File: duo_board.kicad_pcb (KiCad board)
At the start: 2 copper layers, 167 x 122.9 mm, 49 parts, among them J1 PJ-342B-TX-SMT, U1 STM32F103RCTx

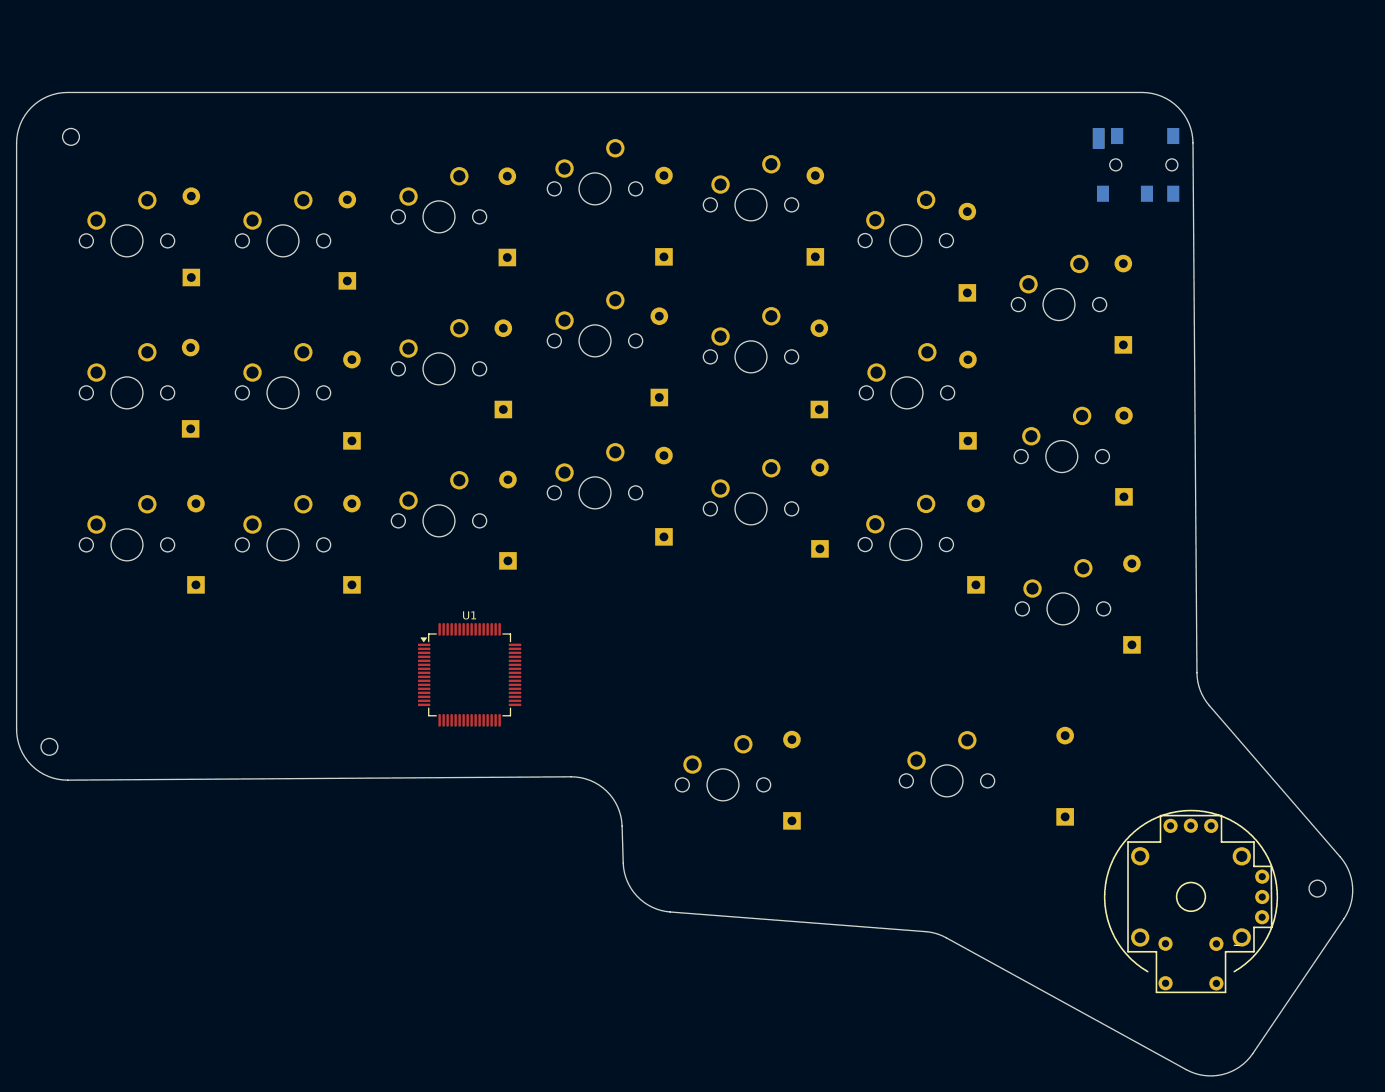
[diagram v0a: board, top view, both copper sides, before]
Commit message: completed MCU power supply
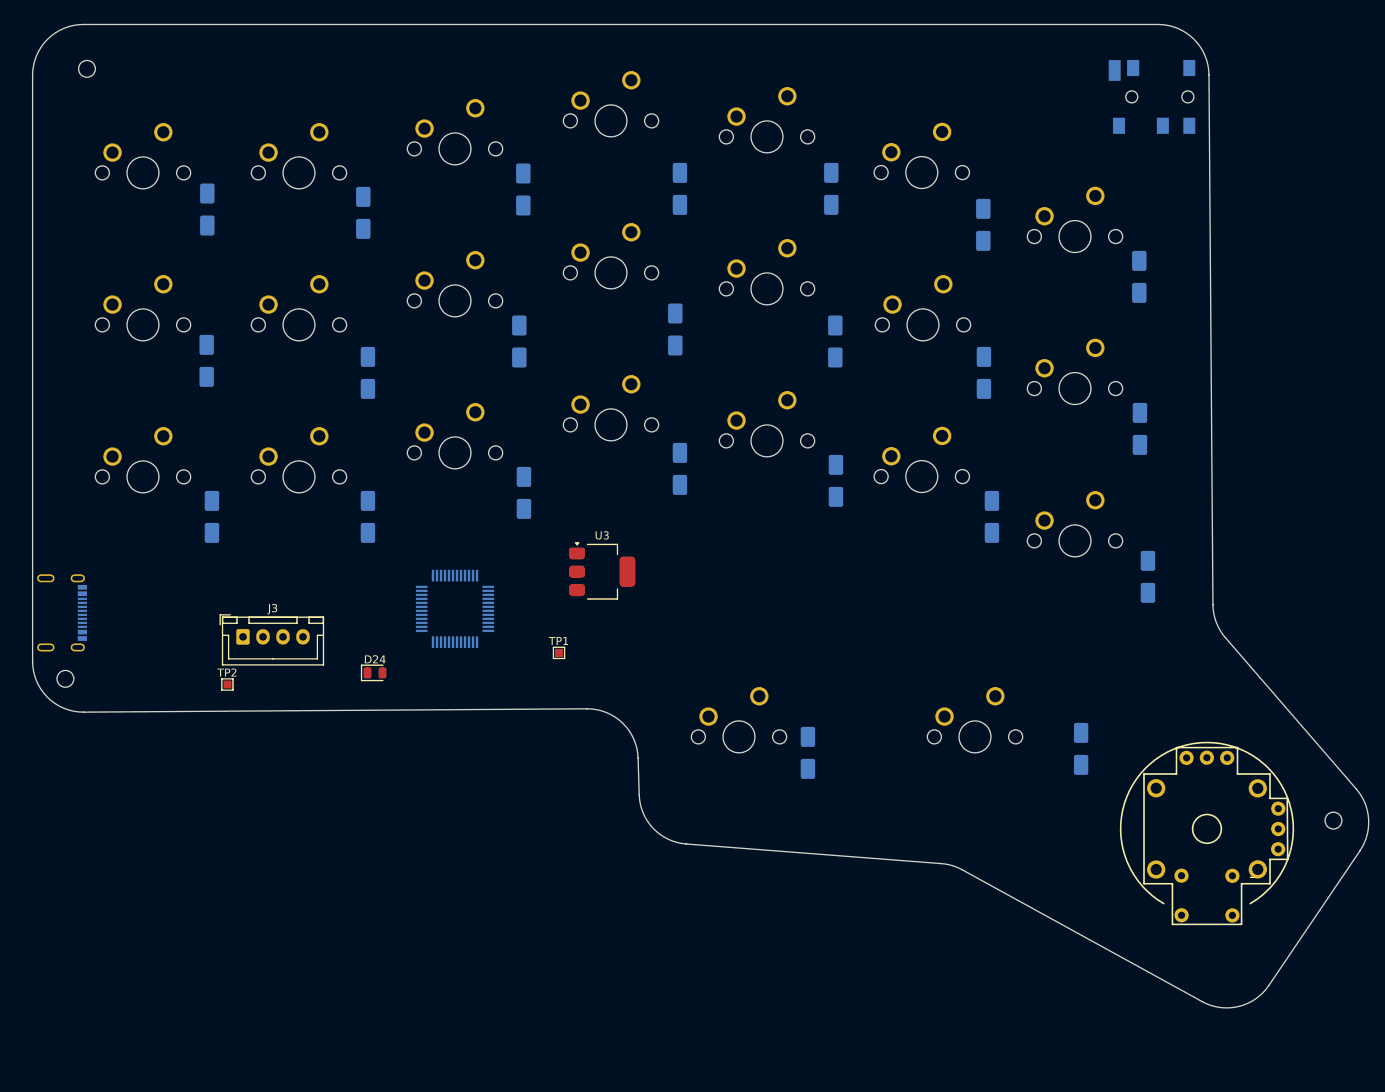
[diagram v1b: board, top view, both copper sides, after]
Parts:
- added D24: LED, LED_SMD:LED_0805_2012Metric, F.Cu at (105.0, 111.0)
- added J2: 2171790001, myCustomLibs:MOLEX_2171790001, B.Cu at (65.0, 103.5)
- added J3: Conn_01x04_Pin, Connector_JST:JST_XH_B4B-XH-A_1x04_P2.50mm_Vertical, F.Cu at (88.5, 106.5)
- added TP1: 5v TP, TestPoint:TestPoint_Pad_1.0x1.0mm, F.Cu at (128.0, 108.5)
- added TP2: 3V TP, TestPoint:TestPoint_Pad_1.0x1.0mm, F.Cu at (86.5, 112.5)
- added U3: AMS1117-3.3, Package_TO_SOT_SMD:SOT-223-3_TabPin2, F.Cu at (133.4, 98.4)
- D1, D10, D11, D12, D13, D14, D15, D16, D17, D18, D19, D2, D20, D21, D22, D23, D3, D4, D5, D6, D7, D8, D9: footprint Diode_THT:D_DO-41_SOD81_P10.16mm_Horizontal -> Diode_SMD:D_SMA
- J1: value PJ-342B-TX-SMT -> TRRS
- MX22: footprint PCM_marbastlib-mx:SW_MX_1.75u -> PCM_marbastlib-mx:SW_MX_1u
- MX23: footprint PCM_marbastlib-mx:SW_MX_1u -> PCM_marbastlib-mx:SW_MX_1.75u
- U1: value STM32F103RCTx -> STM32F103C8Tx; footprint Package_QFP:LQFP-64_10x10mm_P0.5mm -> Package_QFP:LQFP-48_7x7mm_P0.5mm; moved to B.Cu
- moved MX22 34.0 mm to (192.5, 94.5)
- moved MX23 19.4 mm to (180.0, 119.0)
- moved D1 8.73 mm to (84.0, 53.1)
- moved D10 8.73 mm to (123.0, 69.6)
- moved D11 8.73 mm to (142.5, 68.1)
- moved D12 8.73 mm to (162.5, 69.6)
- moved D13 8.73 mm to (181.1, 73.5)
- moved D14 8.73 mm to (200.6, 80.5)
- moved D15 8.73 mm to (84.6, 91.5)
- moved D16 8.73 mm to (104.1, 91.5)
- moved D17 8.73 mm to (123.6, 88.5)
- moved D18 8.73 mm to (143.1, 85.5)
- moved D19 8.73 mm to (162.6, 87.0)
- moved D2 8.73 mm to (103.5, 53.5)
- moved D20 8.73 mm to (182.1, 91.5)
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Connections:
- MX10 pad 1: COL5 -> COL2
- MX10 pad 2: Net-(D13-A) -> Net-(D10-A)
- MX11 pad 1: COL6 -> COL3
- MX11 pad 2: Net-(D14-A) -> Net-(D11-A)
- MX12 pad 1: COL0 -> COL4
- MX12 pad 2: Net-(D15-A) -> Net-(D12-A)
- MX13 pad 1: COL4 -> COL5
- MX13 pad 2: Net-(D5-A) -> Net-(D13-A)
- MX14 pad 1: COL5 -> COL6
- MX14 pad 2: Net-(D6-A) -> Net-(D14-A)
- MX15 pad 1: COL1 -> COL0
- MX15 pad 2: Net-(D16-A) -> Net-(D15-A)
- MX16 pad 1: COL2 -> COL1
- MX16 pad 2: Net-(D17-A) -> Net-(D16-A)
- MX17 pad 1: COL3 -> COL2
- MX17 pad 2: Net-(D18-A) -> Net-(D17-A)
- MX18 pad 1: COL4 -> COL3
- MX18 pad 2: Net-(D19-A) -> Net-(D18-A)
- MX19 pad 1: COL6 -> COL4
- MX19 pad 2: Net-(D7-A) -> Net-(D19-A)
- MX20 pad 1: COL4 -> COL5
- MX20 pad 2: Net-(D22-A) -> Net-(D20-A)
- MX21 pad 1: COL5 -> COL6
- MX21 pad 2: Net-(D20-A) -> Net-(D21-A)
- MX22 pad 1: COL5 -> COL4
- MX22 pad 2: Net-(D23-A) -> Net-(D22-A)
- MX23 pad 1: COL6 -> COL5
- MX23 pad 2: Net-(D21-A) -> Net-(D23-A)
- MX3 pad 1: COL0 -> COL2
- MX3 pad 2: Net-(D8-A) -> Net-(D3-A)
- MX4 pad 1: COL1 -> COL3
- MX4 pad 2: Net-(D9-A) -> Net-(D4-A)
- MX5 pad 1: COL2 -> COL4
- MX5 pad 2: Net-(D10-A) -> Net-(D5-A)
- MX6 pad 1: COL3 -> COL5
- MX6 pad 2: Net-(D11-A) -> Net-(D6-A)
- MX7 pad 1: COL2 -> COL6
- MX7 pad 2: Net-(D3-A) -> Net-(D7-A)
- MX8 pad 1: COL3 -> COL0
- MX8 pad 2: Net-(D4-A) -> Net-(D8-A)
- MX9 pad 1: COL4 -> COL1
- MX9 pad 2: Net-(D12-A) -> Net-(D9-A)
- U1 pad 1: unconnected-(U1-VBAT-Pad1) -> +3.3V
- U1 pad 18: Net-(U1-VSS-Pad18) -> unconnected-(U1-PB0-Pad18)
- U1 pad 23: unconnected-(U1-PA7-Pad23) -> GND
- U1 pad 24: unconnected-(U1-PC4-Pad24) -> +3.3V
- U1 pad 31: Net-(U1-VSS-Pad18) -> unconnected-(U1-PA10-Pad31)
- U1 pad 32: unconnected-(U1-VDD-Pad32) -> /USB_D-
- U1 pad 33: unconnected-(U1-PB12-Pad33) -> /USB_D+
- U1 pad 34: unconnected-(U1-PB13-Pad34) -> /SWDIO
- U1 pad 35: unconnected-(U1-PB14-Pad35) -> GND
- U1 pad 36: unconnected-(U1-PB15-Pad36) -> +3.3V
- U1 pad 37: unconnected-(U1-PC6-Pad37) -> /SWCLK
- U1 pad 44: unconnected-(U1-PA11-Pad44) -> GND
- U1 pad 47: Net-(U1-VSS-Pad18) -> GND
- U1 pad 48: unconnected-(U1-VDD-Pad48) -> +3.3V
- U1 pad 5: unconnected-(U1-PD0-Pad5) -> /HSE_IN
- U1 pad 6: unconnected-(U1-PD1-Pad6) -> /HSE_OUT
- U1 pad 7: unconnected-(U1-NRST-Pad7) -> /NRST
- U1 pad 8: unconnected-(U1-PC0-Pad8) -> GND
- U1 pad 9: unconnected-(U1-PC1-Pad9) -> +3.3V
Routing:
- added copper zone on In2.Cu, net +3.3V
- added copper zone on In1.Cu, net GND
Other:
- copper layers 2 -> 4

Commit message: routed, ready for production?
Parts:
- added C1: 100nF, Capacitor_THT:C_Disc_D4.3mm_W1.9mm_P5.00mm, B.Cu at (102.5, 113.5)
- added C10: 22pF, Capacitor_THT:C_Disc_D3.0mm_W1.6mm_P2.50mm, B.Cu at (124.5, 111.8)
- added C11: 22uF, Capacitor_THT:C_Disc_D4.3mm_W1.9mm_P5.00mm, F.Cu at (82.0, 114.0)
- added C12: 22uF, Capacitor_THT:C_Disc_D4.3mm_W1.9mm_P5.00mm, F.Cu at (92.0, 114.0)
- added C2: 100nF, Capacitor_THT:C_Disc_D4.3mm_W1.9mm_P5.00mm, B.Cu at (123.0, 107.5)
- added C3: 100nF, Capacitor_THT:C_Disc_D4.3mm_W1.9mm_P5.00mm, B.Cu at (102.5, 104.5)
- added C4: 100nF, Capacitor_THT:C_Disc_D4.3mm_W1.9mm_P5.00mm, B.Cu at (118.0, 98.0)
- added C5: 10uF, Capacitor_THT:CP_Radial_Tantal_D5.5mm_P2.50mm, B.Cu at (97.2, 103.0)
- added C6: 10nF, Capacitor_THT:C_Disc_D4.3mm_W1.9mm_P5.00mm, B.Cu at (134.5, 97.5)
- added C7: 1uF, Capacitor_THT:C_Disc_D4.3mm_W1.9mm_P5.00mm, B.Cu at (143.5, 129.0)
- added C8: 100nF, Capacitor_THT:C_Disc_D4.3mm_W1.9mm_P5.00mm, B.Cu at (149.5, 129.5)
- added C9: 22pF, Capacitor_THT:C_Disc_D3.0mm_W1.6mm_P2.50mm, B.Cu at (124.5, 102.8)
- added R1: 1K5, Resistor_THT:R_Axial_DIN0207_L6.3mm_D2.5mm_P10.16mm_Horizontal, B.Cu at (65.0, 77.4)
- added R2: 1K5, Resistor_THT:R_Axial_DIN0207_L6.3mm_D2.5mm_P10.16mm_Horizontal, F.Cu at (169.9, 130.5)
- added Y1: 16Mhz, Crystal:Crystal_HC49-4H_Vertical, B.Cu at (133.5, 106.0)
- moved MX12 81.9 mm to (154.0, 61.5)
- moved MX7 78.7 mm to (193.0, 56.0)
- moved J3 73.1 mm to (92.2, 33.5)
- moved MX8 64.0 mm to (76.0, 68.0)
- moved D24 61.6 mm to (163.4, 130.5), turned to 180 degrees
- moved TP2 60.2 mm to (144.0, 94.5)
- moved MX11 59.7 mm to (134.5, 61.5)
- moved MX9 58.7 mm to (95.5, 68.0)
- moved MX10 58.6 mm to (115.0, 65.0)
- moved TP1 56.2 mm to (72.0, 113.5)
- moved U3 51.1 mm to (82.5, 103.0), turned to 90 degrees
- moved MX4 46.6 mm to (134.5, 42.0)
- moved MX19 45.9 mm to (154.0, 81.5)
- moved MX5 45.0 mm to (154.0, 42.0)
- moved MX3 44.8 mm to (115.0, 45.5)
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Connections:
- J1 pad 2: unconnected-(J1-Pad2) -> USART1_RX
- J1 pad 3: unconnected-(J1-Pad3) -> USART1_TX
- J1 pad 4: unconnected-(J1-Pad4) -> USART1_TX
- J1 pad 5: unconnected-(J1-Pad5) -> GND
- J1 pad 6: unconnected-(J1-Pad6) -> +3.3V
- J1 pad 7: unconnected-(J1-Pad7) -> +3.3V
- U1 pad 18: unconnected-(U1-PB0-Pad18) -> /X_AXIS
- U1 pad 19: unconnected-(U1-PB1-Pad19) -> /Y_AXIS
- U1 pad 28: unconnected-(U1-PB15-Pad28) -> /BTN_PIN
- U1 pad 30: unconnected-(U1-PA9-Pad30) -> USART1_TX
- U1 pad 31: unconnected-(U1-PA10-Pad31) -> USART1_RX
- U2 pad B1A: unconnected-(U2-SEL+-PadB1A) -> /BTN_PIN
- U2 pad B2A: unconnected-(U2-SEL--PadB2A) -> GND
- U2 pad H1: unconnected-(U2-H+-PadH1) -> GND
- U2 pad H2: unconnected-(U2-H-PadH2) -> /Y_AXIS
- U2 pad H3: unconnected-(U2-H--PadH3) -> +3.3V
- U2 pad S1: Net-(U2-SHIELD-PadS1) -> GND
- U2 pad S2: Net-(U2-SHIELD-PadS1) -> GND
- U2 pad S3: Net-(U2-SHIELD-PadS1) -> GND
- U2 pad S4: Net-(U2-SHIELD-PadS1) -> GND
- U2 pad V1: unconnected-(U2-V+-PadV1) -> +3.3V
- U2 pad V2: unconnected-(U2-V-PadV2) -> /X_AXIS
- U2 pad V3: unconnected-(U2-V--PadV3) -> GND
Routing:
- net ROW0: track 0.00 -> 193.5 mm, vias 0 -> 2
- net USART1_TX: track 0.00 -> 158.8 mm, vias 0 -> 2
- net USART1_RX: track 0.00 -> 152.4 mm, vias 0 -> 2
- net +3.3V: track 0.00 -> 152.1 mm, vias 0 -> 15
- net ROW2: track 0.00 -> 146.0 mm, vias 0 -> 2
- net ROW1: track 0.00 -> 142.8 mm, vias 0 -> 2
- net /BTN_PIN: track 0.00 -> 114.3 mm, vias 0 -> 1
- net /X_AXIS: track 0.00 -> 112.3 mm, vias 0 -> 1
- net /Y_AXIS: track 0.00 -> 102.2 mm, vias 0 -> 1
- net /SWDIO: track 0.00 -> 86.5 mm
- net /SWCLK: track 0.00 -> 79.3 mm
- net COL5: track 0.00 -> 73.5 mm
- net /USB_D+: track 0.00 -> 66.2 mm
- net COL4: track 0.00 -> 65.9 mm
- net GND: track 0.00 -> 53.3 mm, vias 0 -> 7
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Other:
- board text added: "GED-DUO-BOARD"

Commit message: added firmware submodule and updated pcb
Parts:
- added TP3: GND TP, TestPoint:TestPoint_Pad_1.0x1.0mm, F.Cu at (155.5, 94.0)
- moved TP1 7.50 mm to (72.0, 106.0)
- moved C1 0.50 mm to (102.5, 114.0)
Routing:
- net +5V: track 37.4 -> 32.7 mm, vias 1 -> 2
- net GND: track 53.3 -> 48.6 mm
- net +3.3V: track 152.1 -> 149.3 mm, vias 15 -> 14
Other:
- outline, holes or cut-outs redrawn
